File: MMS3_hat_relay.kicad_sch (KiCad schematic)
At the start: 12 parts, among them U4 AMS1117

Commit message: done
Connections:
- no-connect marks 2 -> 18
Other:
- removed sheet Power Connector
- added sheet CH32V003 (CH32V003.kicad_sch)
- added sheet Relay 1 (Quick_n_dirty_relay.kicad_sch)
- added sheet Relay 2 (Quick_n_dirty_relay.kicad_sch)
- added sheet Relay 3 (Quick_n_dirty_relay.kicad_sch)
- added sheet Relay 4 (Quick_n_dirty_relay.kicad_sch)
- added sheet Relay 5 (Quick_n_dirty_relay.kicad_sch)
- title: MMS3 Hat template small (Change Me) -> MMS3 Hat Relay

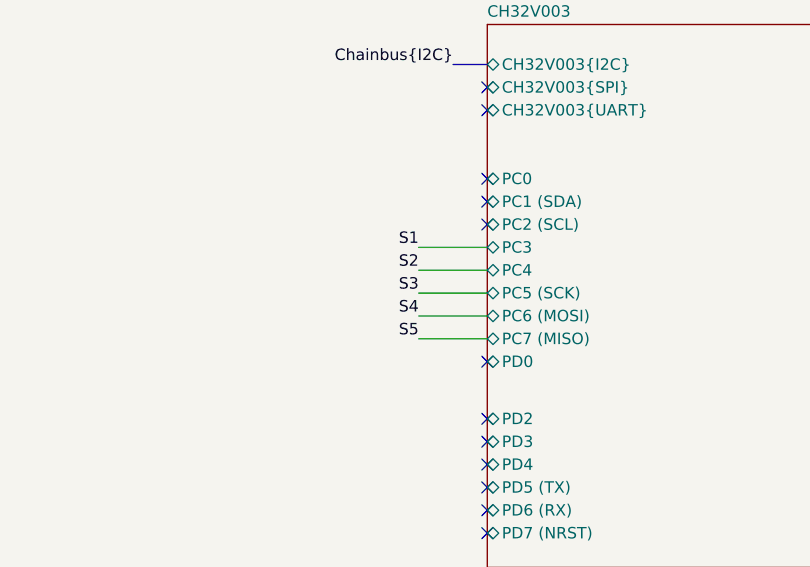
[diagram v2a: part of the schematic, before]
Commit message: changed headers and relays to better one
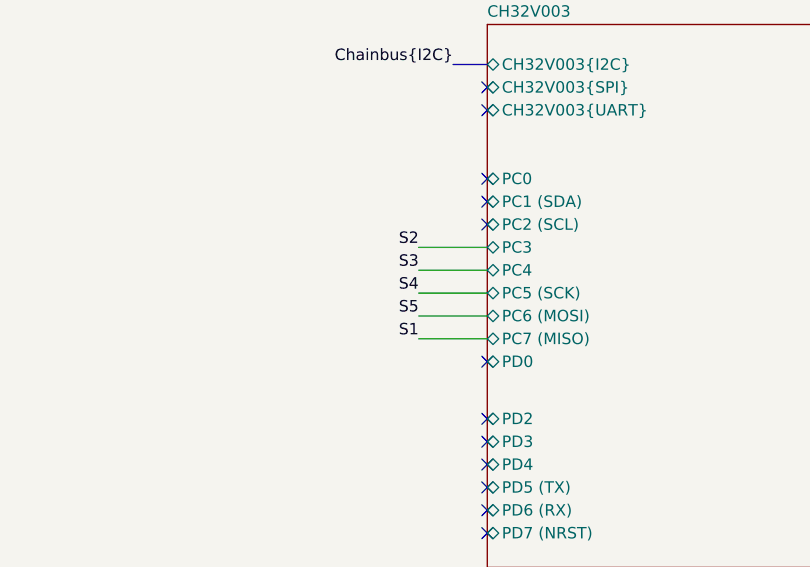
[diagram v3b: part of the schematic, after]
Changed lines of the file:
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@@
 		)
 	)
-	(label "S1"
+	(label "S2"
 		(at 226.06 113.03 180)
 		(effects
@@
 		)
 	)
-	(label "S3"
+	(label "S4"
 		(at 226.06 118.11 180)
 		(effects
@@
 		)
 	)
-	(label "S4"
+	(label "S5"
 		(at 226.06 120.65 180)
-		(effects
-			(font
-				(size 1.27 1.27)
-			)
-			(justify right bottom)
-		)
-	)
-	(label "S2"
-		(at 226.06 115.57 180)
-		(effects
-			(font
-				(size 1.27 1.27)
-			)
-			(justify right bottom)
-		)
-	)
-	(label "S5"
-		(at 226.06 123.19 180)
 		(effects
 			(font
@@
 	(label "S1"
 		(at 27.94 111.76 180)
+		(effects
+			(font
+				(size 1.27 1.27)
+			)
+			(justify right bottom)
+		)
+	)
+	(label "S3"
+		(at 226.06 115.57 180)
 		(effects
 			(font
@@
 		(effects
 			(font
+				(size 1.27 1.27)
+			)
+			(justify right bottom)
+		)
+	)
+	(label "S1"
+		(at 226.06 123.19 180)
+		(effects
+			(font
